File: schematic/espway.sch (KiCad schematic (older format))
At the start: 31 parts, among them J1 CONN_01X02, J2 CONN_01X02, J3 CONN_01X04_MALE, SW1 SW_Push, U1 DRV8835, U2 LM1117-3.3, U3 ESP-12E, U4 LSM6DS3

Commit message: Aesthetic changes to PCB
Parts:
- BT1: footprint Wire_Connections_Bridges:WireConnection_1.00mmDrill -> Wire_Connections_Bridges:WireConnection_1.20mmDrill
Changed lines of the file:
@@
 F 0 "BT1" H 5100 1500 50  0000 L CNN
 F 1 "4.8V (4*AAA NiMH)" H 5100 1400 50  0000 L CNN
-F 2 "Wire_Connections_Bridges:WireConnection_1.00mmDrill" V 5000 1460 50  0001 C CNN
+F 2 "Wire_Connections_Bridges:WireConnection_1.20mmDrill" V 5000 1460 50  0001 C CNN
 F 3 "" V 5000 1460 50  0001 C CNN
 	1    5000 1400

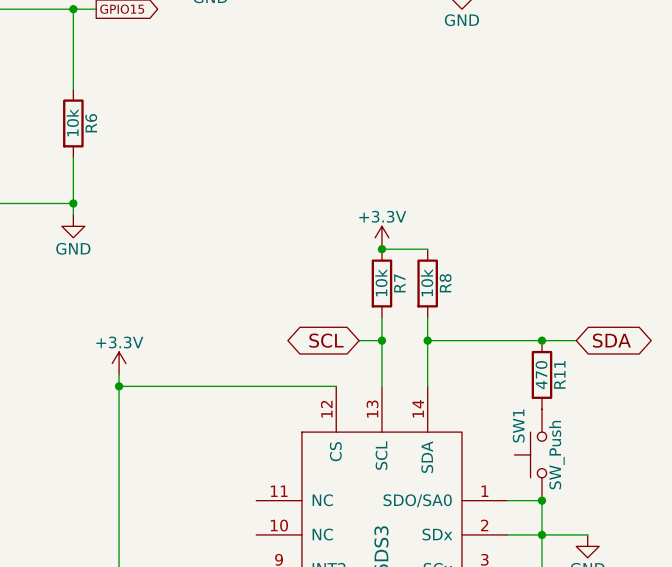
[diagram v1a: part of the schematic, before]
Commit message: Decrease I2C pullups to 2k2 (UNTESTED but should work better)
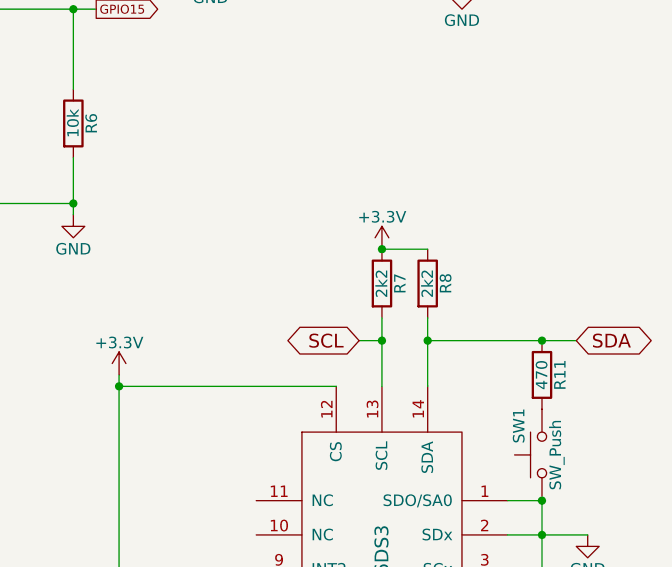
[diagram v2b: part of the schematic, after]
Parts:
- R7, R8: value 10k -> 2k2
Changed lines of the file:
@@
 P 8800 4150
 F 0 "R7" V 8880 4150 50  0000 C CNN
-F 1 "10k" V 8800 4150 50  0000 C CNN
+F 1 "2k2" V 8800 4150 50  0000 C CNN
 F 2 "Resistors_SMD:R_0603" V 8730 4150 50  0001 C CNN
 F 3 "" H 8800 4150 50  0001 C CNN
@@
 P 9000 4150
 F 0 "R8" V 9080 4150 50  0000 C CNN
-F 1 "10k" V 9000 4150 50  0000 C CNN
+F 1 "2k2" V 9000 4150 50  0000 C CNN
 F 2 "Resistors_SMD:R_0603" V 8930 4150 50  0001 C CNN
 F 3 "" H 9000 4150 50  0001 C CNN

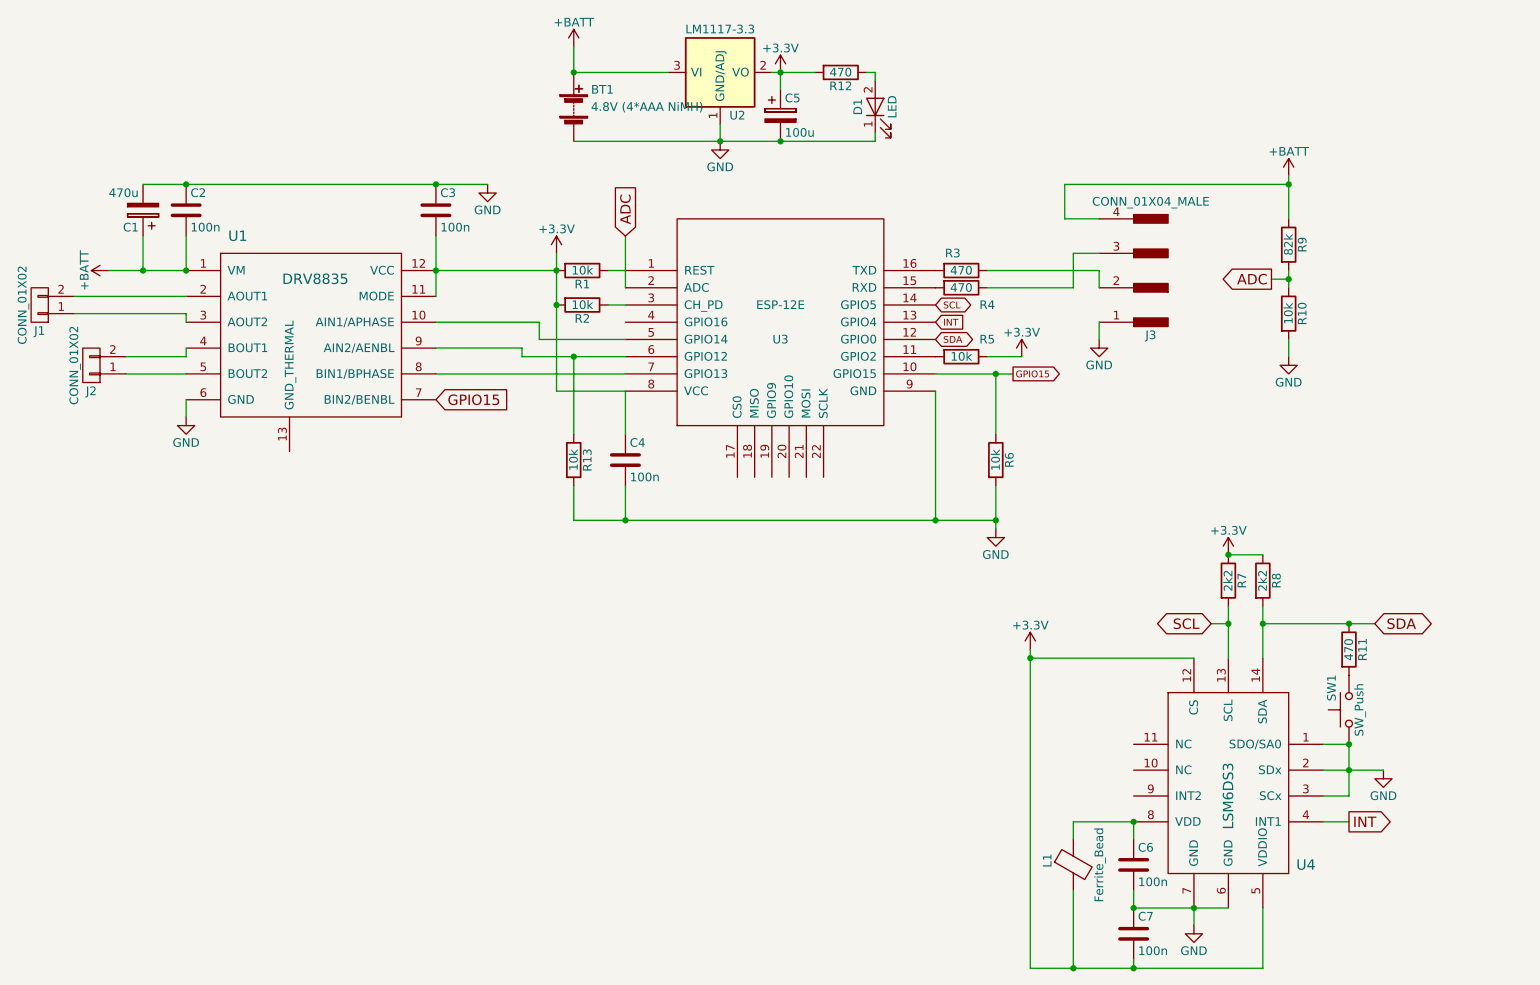
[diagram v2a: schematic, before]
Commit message: PCB: improvements
Routing simplified
Use LGA-14 and WSON-12 packages supplied with KiCAD
diff --git a/schematic-old/espway-rescue.lib b/schematic-old/espway-rescue.lib
new file mode 100644
index 0000000..4d5fc14
--- /dev/null
+++ b/schematic-old/espway-rescue.lib
@@ -0,0 +1,25 @@
+EESchema-LIBRARY Version 2.3
+#encoding utf-8
+#
+# LM1117-5.0-RESCUE-espway
+#
+DEF LM1117-5.0-RESCUE-espway U 0 30 Y Y 1 F N
+F0 "U" 100 -250 50 H V C CNN
+F1 "LM1117-5.0-RESCUE-espway" 0 250 50 H V C CNN
+F2 "" 0 0 50 H V C CNN
+F3 "" 0 0 50 H V C CNN
+$FPLIST
+ SOT-223*
+ TO-263*
+ TO-252*
+$ENDFPLIST
+DRAW
+S -200 -200 200 200 0 1 10 f
+X GND/ADJ 1 0 -300 100 U 50 50 1 1 W
+X VO 2 300 0 100 L 50 50 1 1 w
+X VI 3 -300 0 100 R 50 50 1 1 W
+X VO 4 300 0 100 L 50 50 1 1 w N
+ENDDRAW
+ENDDEF
+#
+#End Library
diff --git a/schematic-old/espway.pro b/schematic-old/espway.pro
index d39d63e..2c69b71 100644
--- a/schematic-old/espway.pro
+++ b/schematic-old/espway.pro
@@ -1,4 +1,4 @@
-update=su  5. helmikuuta 2017 09.41.29
+update=2017 October 17, Tuesday 01:25:24
 version=1
 last_client=kicad
 [pcbnew]
@@ -25,43 +25,6 @@ version=1
 NetIExt=net
 [general]
 version=1
-[eeschema]
-version=1
-LibDir=
-[eeschema/libraries]
-LibName1=power
-LibName2=device
-LibName3=transistors
-LibName4=conn
-LibName5=linear
-LibName6=regul
-LibName7=74xx
-LibName8=cmos4000
-LibName9=adc-dac
-LibName10=memory
-LibName11=xilinx
-LibName12=microcontrollers
-LibName13=dsp
-LibName14=microchip
-LibName15=analog_switches
-LibName16=motorola
-LibName17=texas
-LibName18=intel
-LibName19=audio
-LibName20=interface
-LibName21=digital-audio
-LibName22=philips
-LibName23=display
-LibName24=cypress
-LibName25=siliconi
-LibName26=opto
-LibName27=atmel
-LibName28=contrib
-LibName29=valves
-LibName30=d1_mini
-LibName31=gy-521
-LibName32=ws2812b
-LibName33=l293d
 [schematic_editor]
 version=1
 PageLayoutDescrFile=
@@ -72,3 +35,41 @@ NetFmtName=
 SpiceForceRefPrefix=0
 SpiceUseNetNumbers=0
 LabSize=60
+[eeschema]
+version=1
+LibDir=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
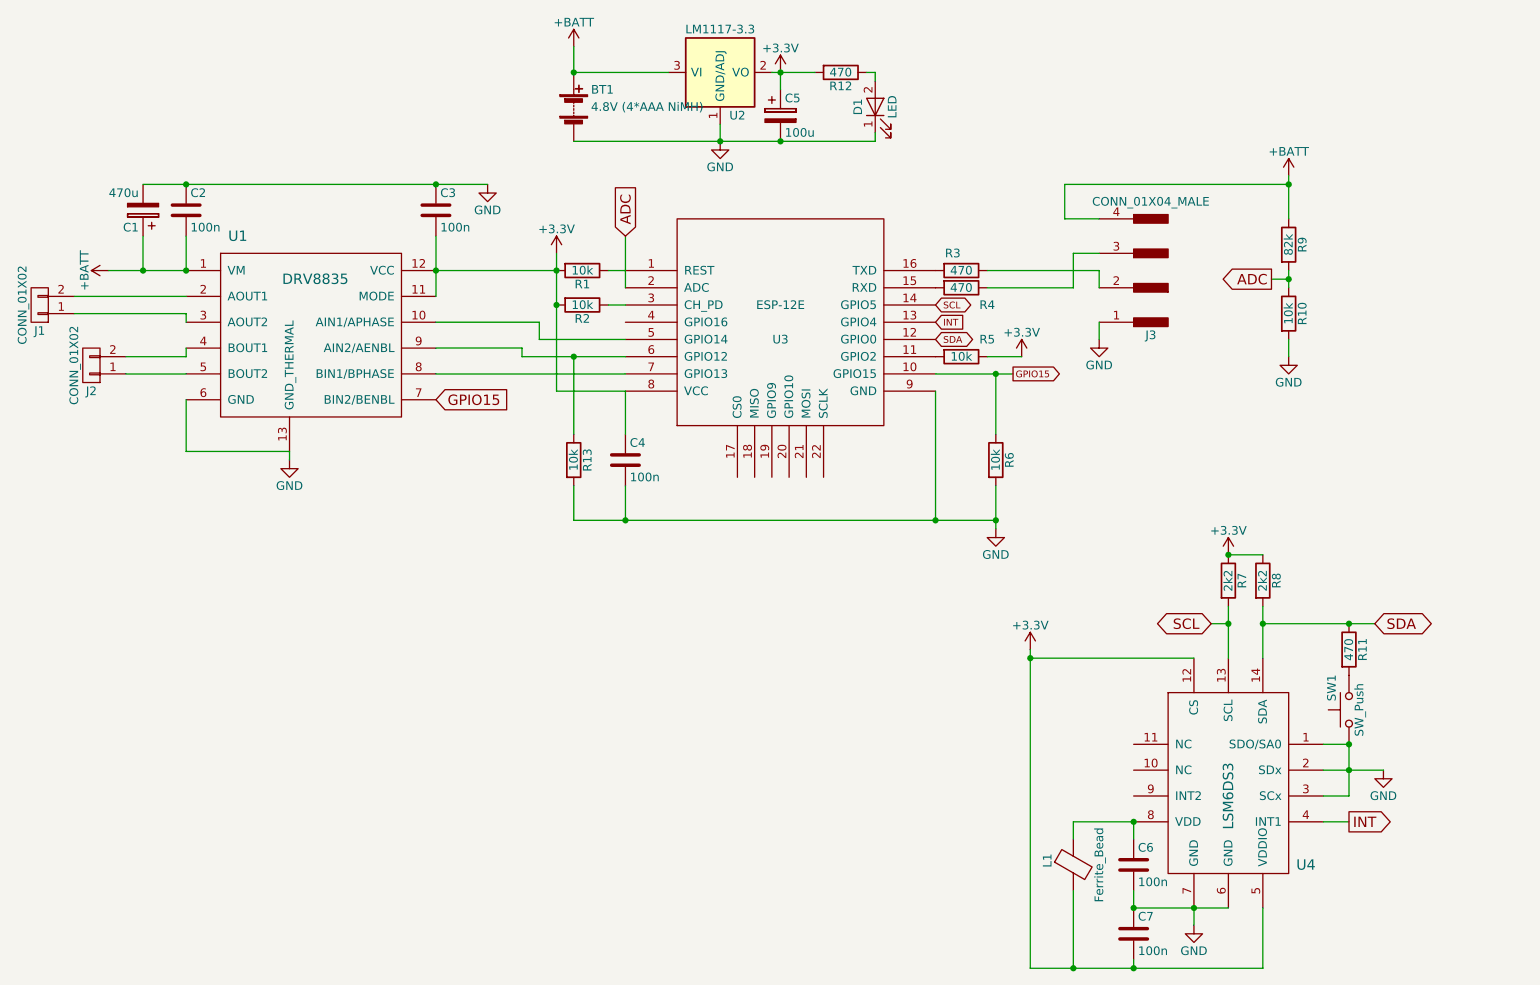
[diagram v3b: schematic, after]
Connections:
- net GND: now also U1.13 (GND_THERMAL)
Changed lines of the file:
@@
 GPIO15
-$Comp
-L GND #PWR012
-U 1 1 59BA5B49
-P 2750 3200
-F 0 "#PWR012" H 2750 2950 50  0001 C CNN
-F 1 "GND" H 2750 3050 50  0000 C CNN
-F 2 "" H 2750 3200 50  0001 C CNN
-F 3 "" H 2750 3200 50  0001 C CNN
-	1    2750 3200
-	1    0    0    -1
-$EndComp
 $Comp
 L Battery BT1
@@
 Connection ~ 7450 3800
 Wire Wire Line
-	7100 3050 7100 3800
+	7100 3800 7100 3050
 Wire Wire Line
 	5300 2350 5200 2350
@@
 	9000 6400 9000 6050
 Wire Wire Line
-	8250 6350 8250 6400
+	8250 6400 8250 6350
 Connection ~ 8250 6400
 Connection ~ 8250 6050
@@
 Connection ~ 4200 2350
 Connection ~ 7450 2950
-Wire Wire Line
-	2750 3200 2750 3100
 Connection ~ 5850 1600
 Wire Wire Line
@@
 	5000 3600 5000 3800
 Connection ~ 5300 3800
+Wire Wire Line
+	2750 3100 2750 3400
+Wire Wire Line
+	2750 3400 3350 3400
+$Comp
+L GND #PWR?
+U 1 1 5A19A5EC
+P 3350 3450
+F 0 "#PWR?" H 3350 3200 50  0001 C CNN
+F 1 "GND" H 3350 3300 50  0000 C CNN
+F 2 "" H 3350 3450 50  0001 C CNN
+F 3 "" H 3350 3450 50  0001 C CNN
+	1    3350 3450
+	1    0    0    -1
+$EndComp
+Wire Wire Line
+	3350 3400 3350 3450
 $EndSCHEMATC

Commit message: PCB update before rerouting
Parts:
- removed R5: 10k, Resistors_SMD:R_0603, symbol R
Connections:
- net SCL: now also U3.11 (GPIO2); no longer U3.14 (GPIO5)
- net at R3.1: now also J3.3; no longer J3.2
- net at R4.1: now also J3.2; no longer J3.3
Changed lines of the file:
@@
 Text GLabel 9050 2400 0    60   Output ~ 0
 ADC
-Text GLabel 7100 2550 2    39   BiDi ~ 0
-SCL
 Text GLabel 7100 2650 2    39   Input ~ 0
 INT
@@
 Text GLabel 8700 4400 0    60   BiDi ~ 0
 SCL
-Text GLabel 9650 4400 2    60   BiDi ~ 0
+Text GLabel 9600 4400 2    60   BiDi ~ 0
 SDA
 $Comp
@@
 Connection ~ 2500 2350
 $Comp
-L +BATT #PWR013
+L +BATT #PWR012
 U 1 1 59BA76F1
 P 5000 1050
-F 0 "#PWR013" H 5000 900 50  0001 C CNN
+F 0 "#PWR012" H 5000 900 50  0001 C CNN
 F 1 "+BATT" H 5000 1190 50  0000 C CNN
 F 2 "" H 5000 1050 50  0001 C CNN
@@
 	5000 1200 5550 1200
 $Comp
-L +BATT #PWR014
+L +BATT #PWR013
 U 1 1 59BA7893
 P 9150 1800
-F 0 "#PWR014" H 9150 1650 50  0001 C CNN
+F 0 "#PWR013" H 9150 1650 50  0001 C CNN
 F 1 "+BATT" H 9150 1940 50  0000 C CNN
 F 2 "" H 9150 1800 50  0001 C CNN
@@
 $EndComp
 $Comp
-L +BATT #PWR015
+L +BATT #PWR014
 U 1 1 59BA7C2C
 P 2300 2350
-F 0 "#PWR015" H 2300 2200 50  0001 C CNN
+F 0 "#PWR014" H 2300 2200 50  0001 C CNN
 F 1 "+BATT" H 2300 2490 50  0000 C CNN
 F 2 "" H 2300 2350 50  0001 C CNN
@@
 Connection ~ 2750 2350
 Connection ~ 5000 1200
-$Comp
-L R R5
-U 1 1 59BB0CA5
-P 7250 2850
-F 0 "R5" V 7150 3000 50  0000 C CNN
-F 1 "10k" V 7250 2850 50  0000 C CNN
-F 2 "Resistors_SMD:R_0603" V 7180 2850 50  0001 C CNN
-F 3 "" H 7250 2850 50  0001 C CNN
-	1    7250 2850
-	0    1    1    0
-$EndComp
-$Comp
-L +3.3V #PWR016
-U 1 1 59BB0EE7
-P 7600 2850
-F 0 "#PWR016" H 7600 2700 50  0001 C CNN
-F 1 "+3.3V" H 7600 2990 50  0000 C CNN
-F 2 "" H 7600 2850 50  0001 C CNN
-F 3 "" H 7600 2850 50  0001 C CNN
-	1    7600 2850
-	1    0    0    -1
-$EndComp
-Wire Wire Line
-	7600 2850 7400 2850
 Wire Wire Line
 	9000 4000 8800 4000
@@
 Wire Wire Line
 	8800 4300 8800 4600
-Wire Wire Line
-	9000 4300 9000 4600
-Wire Wire Line
-	9000 4400 9650 4400
-Connection ~ 9500 4400
-Connection ~ 9000 4400
 Connection ~ 8800 4400
 Connection ~ 9500 5100
@@
 	6750 1600 6750 1550
 Connection ~ 6200 1600
-Wire Wire Line
-	7400 2450 7900 2450
-Wire Wire Line
-	7900 2450 7900 2250
-Wire Wire Line
-	7900 2250 8050 2250
-Wire Wire Line
-	7400 2350 8050 2350
-Wire Wire Line
-	8050 2350 8050 2450
 $Comp
 L R R13
@@
 	2750 3400 3350 3400
 $Comp
-L GND #PWR?
+L GND #PWR016
 U 1 1 5A19A5EC
 P 3350 3450
-F 0 "#PWR?" H 3350 3200 50  0001 C CNN
+F 0 "#PWR016" H 3350 3200 50  0001 C CNN
 F 1 "GND" H 3350 3300 50  0000 C CNN
 F 2 "" H 3350 3450 50  0001 C CNN
@@
 Wire Wire Line
 	3350 3400 3350 3450
+Wire Wire Line
+	9000 4300 9000 4600
+Connection ~ 9000 4400
+Wire Wire Line
+	8050 2450 7400 2450
+Wire Wire Line
+	7400 2350 8050 2350
+Wire Wire Line
+	8050 2350 8050 2250
+Text GLabel 7100 2850 2    39   BiDi ~ 0
+SCL
+Wire Wire Line
+	9000 4400 9600 4400
+Connection ~ 9500 4400
 $EndSCHEMATC

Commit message: Initial work on new PCB
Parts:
- added R4, R9: 10k, Resistors_SMD:R_0603, symbol R
- U3: renamed from U1; footprint espway-modules:WSON-12 -> Housings_SON:WSON-12-1EP_3x2mm_Pitch0.5mm_ThermalVias
- U4: footprint espway-modules:LGA-14L -> Housings_LGA:Bosch_LGA-14_3x2.5mm_Pitch0.5mm
- renumbered C4 to C1, C1 to C2, C2 to C3, C5 to C4, C3 to C5, R11 to R10, R9 to R11, R10 to R12, R7 to R13, R8 to R14, R12 to R3, R3 to R5, R4 to R6, R13 to R7, R6 to R8, U2 to U1, U3 to U2
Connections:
- net +3V3: now also R9.1
- net GND: now also R10.2, R4.2; no longer SW1.1
- net INT: now also U2.5 (GPIO14); no longer U2.13 (GPIO4)
- net SCL: now also U2.7 (GPIO13); no longer U2.11 (GPIO2)
- net SDA: now also U2.6 (GPIO12); no longer R10.1, U2.12 (GPIO0)
- net APHASE: now reaches U3.10 (AIN1/APHASE)
- net APHASE: now also R8.1, U2.10 (GPIO15); no longer U2.5 (GPIO14)
- net AENBL: now reaches R7.1, U3.9 (AIN2/AENBL)
- net AENBL: now also U2.11 (GPIO2); no longer U2.6 (GPIO12)
- net BPHASE: now reaches U3.8 (BIN1/BPHASE)
- net BPHASE: now also SW1.2, U2.12 (GPIO0), R9.2; no longer U2.7 (GPIO13)
- removed net GPIO15: R8.1, U2.10 (GPIO15), U3.7 (BIN2/BENBL)
- new net: R10.1, SW1.1
- new net BENBL: R4.1, U2.13 (GPIO4), U3.7 (BIN2/BENBL)
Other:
- moved on the sheet: C1, C2, C3, C5, C6, C7, J1, J2, J3, L1, R10, R11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

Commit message: An intermediate commit
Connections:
- net INT: now also U2.7 (GPIO13); no longer U2.5 (GPIO14)
- net SCL: now also U2.5 (GPIO14); no longer U2.7 (GPIO13)
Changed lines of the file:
@@
 Text GLabel 8750 2750 0    60   Output ~ 0
 ADC
-Text GLabel 5300 2750 0    39   Input ~ 0
-INT
+Text GLabel 5300 2750 0    39   BiDi ~ 0
+SCL
 Text GLabel 5300 2850 0    39   BiDi ~ 0
 SDA
@@
 	9700 3850 9700 4150
 Connection ~ 9700 3950
-Text GLabel 5300 2950 0    39   BiDi ~ 0
-SCL
+Text GLabel 5300 2950 0    39   Input ~ 0
+INT
 $Comp
 L +3V3 #PWR016
